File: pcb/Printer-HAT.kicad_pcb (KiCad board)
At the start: 2 copper layers, 65 x 56 mm, 38 parts, among them J1 Screw_Terminal, J4 Conn_01x03_Male, K1 SRD-05VDC-SL-C, K2 SLA-05VDC-SL-C, P1 Conn_02x20_Odd_Even, Q2 S8050, Q3 S8050, Q4 Q_Dual_PNP_PNP_C1B1B2C2E2E1, Q5 DMG2305UX-7, U1 LM2596S-5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

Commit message: fix issues with initial pcb
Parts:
- removed Q3: S8050, Package_TO_SOT_SMD:SOT-23
- added Q1: S8050, Package_TO_SOT_SMD:SOT-23, F.Cu at (207.9, 121.7)
- R3: value 3K -> 1K
- moved R5 49.8 mm to (252.3, 108.6), turned to 180 degrees
- moved D4 49.8 mm to (252.3, 106.8), turned to 180 degrees
- moved R3 43.1 mm to (214.8, 103.3)
- moved Q2 33.3 mm to (237.1, 105.6), turned to 0 degrees
- moved R4 20.8 mm to (247.5, 105.5), turned to -90 degrees
- moved D6 9.70 mm to (245.7, 105.6), turned to 90 degrees
- moved D5 6.09 mm to (211.4, 103.3), turned to 0 degrees
- moved J4 3.03 mm to (202.5, 108.6), turned to 180 degrees
- moved R6 2.98 mm to (206.9, 106.8), turned to -90 degrees
- moved D3 2.38 mm to (258.7, 124.6)
- moved R11 1.39 mm to (243.9, 102.4), turned to -90 degrees
- moved R7 1.22 mm to (232.7, 103.0)
- moved R9 1.20 mm to (232.7, 101.5)
- moved U3 0.54 mm to (238.6, 102.2)
- moved D8 0.14 mm to (241.9, 105.9)
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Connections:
- D5 pad 1: /GPIO17(GEN0) -> Net-(K2-Pad5)
- D6 pad 1: /GPIO27(GEN2) -> Net-(D8-Pad2)
- D7 pad 2: Net-(D7-Pad2) -> Net-(K2-Pad5)
- J4 pad 1: /GPIO4(GCLK) -> /GPIO14(TXD0)
- K1 pad 4: /AUX_PWR -> unconnected-(K1-Pad4)
- K1 pad 5: unconnected-(K1-Pad5) -> /AUX_PWR
- K2 pad 5: Net-(D7-Pad2) -> Net-(K2-Pad5)
- Q2 pad 1: GND -> Net-(Q2-Pad1)
- Q2 pad 2: Net-(Q2-Pad2) -> GND
- Q2 pad 3: Net-(D7-Pad2) -> Net-(D8-Pad2)
- R10 pad 2: Net-(Q2-Pad2) -> Net-(Q1-Pad1)
- R11 pad 2: Net-(Q3-Pad2) -> Net-(Q2-Pad1)
- R3 pad 1: +5VD -> Net-(D5-Pad2)
- R3 pad 2: Net-(R3-Pad2) -> +5V
- R4 pad 1: Net-(R3-Pad2) -> Net-(D6-Pad2)
- R4 pad 2: GND -> +5V
- U1 pad 4: Net-(R3-Pad2) -> +5VD
- U2 pad 2: Net-(D5-Pad2) -> /GPIO17(GEN0)
- U3 pad 2: Net-(D6-Pad2) -> /GPIO27(GEN2)
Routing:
- net Net-(K2-Pad5): track 0.00 -> 54.9 mm, vias 0 -> 1
- net +5V: track 186.8 -> 140.4 mm, vias 10 -> 3
- net Net-(D7-Pad2): track 32.8 -> 0.00 mm, vias 1 -> 0
- net /GPIO14(TXD0): track 0.00 -> 22.3 mm
- net /GPIO4(GCLK): track 18.6 -> 0.00 mm, vias 1 -> 0
- net +5VD: track 23.7 -> 37.6 mm
- net Net-(R3-Pad2): track 13.6 -> 0.00 mm
- net Net-(Q2-Pad1): track 0.00 -> 8.38 mm
- net GND: track 55.2 -> 50.5 mm, vias 76 -> 83
- net Net-(D8-Pad2): track 21.6 -> 17.9 mm, vias 1 -> 0
- net Net-(Q2-Pad2): track 3.41 -> 0.00 mm
- net /GPIO17(GEN0): track 25.2 -> 22.2 mm, vias 2 -> 0
- net /GPIO27(GEN2): track 19.8 -> 16.8 mm, vias 1 -> 0
- net Net-(D6-Pad2): track 4.19 -> 1.80 mm
- net Net-(Q1-Pad1): track 0.00 -> 2.38 mm
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
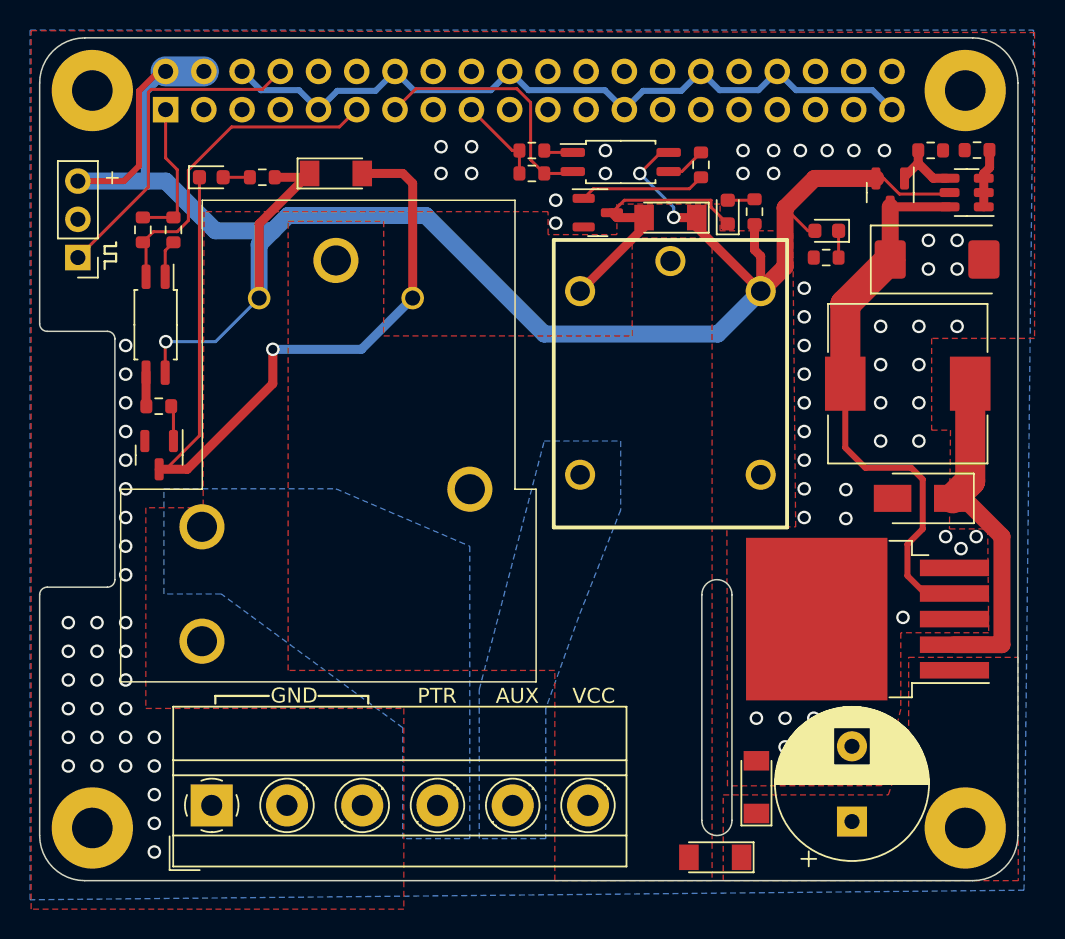
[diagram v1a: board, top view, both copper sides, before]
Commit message: fix PCB DRC errors
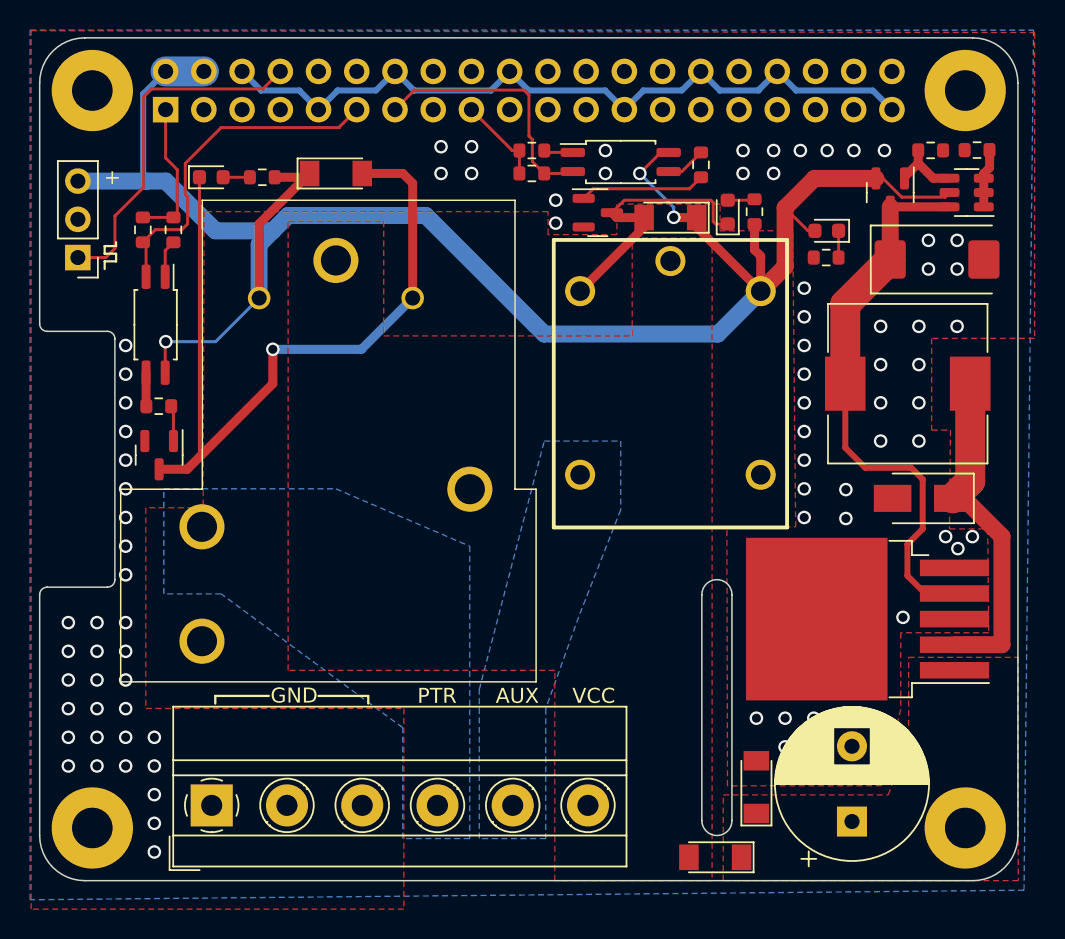
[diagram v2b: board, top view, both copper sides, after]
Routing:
- net +5V: track 140.4 -> 129.0 mm
- net Net-(K2-Pad5): track 54.9 -> 52.7 mm
- net /GPIO14(TXD0): track 22.3 -> 23.4 mm
- net /GPIO17(GEN0): track 22.2 -> 22.8 mm
